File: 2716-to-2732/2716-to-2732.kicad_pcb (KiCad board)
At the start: 2 copper layers, 21.9 x 40.6 mm, 4 parts, among them J1 2716, J2 2732, SW1 A_{11} Select

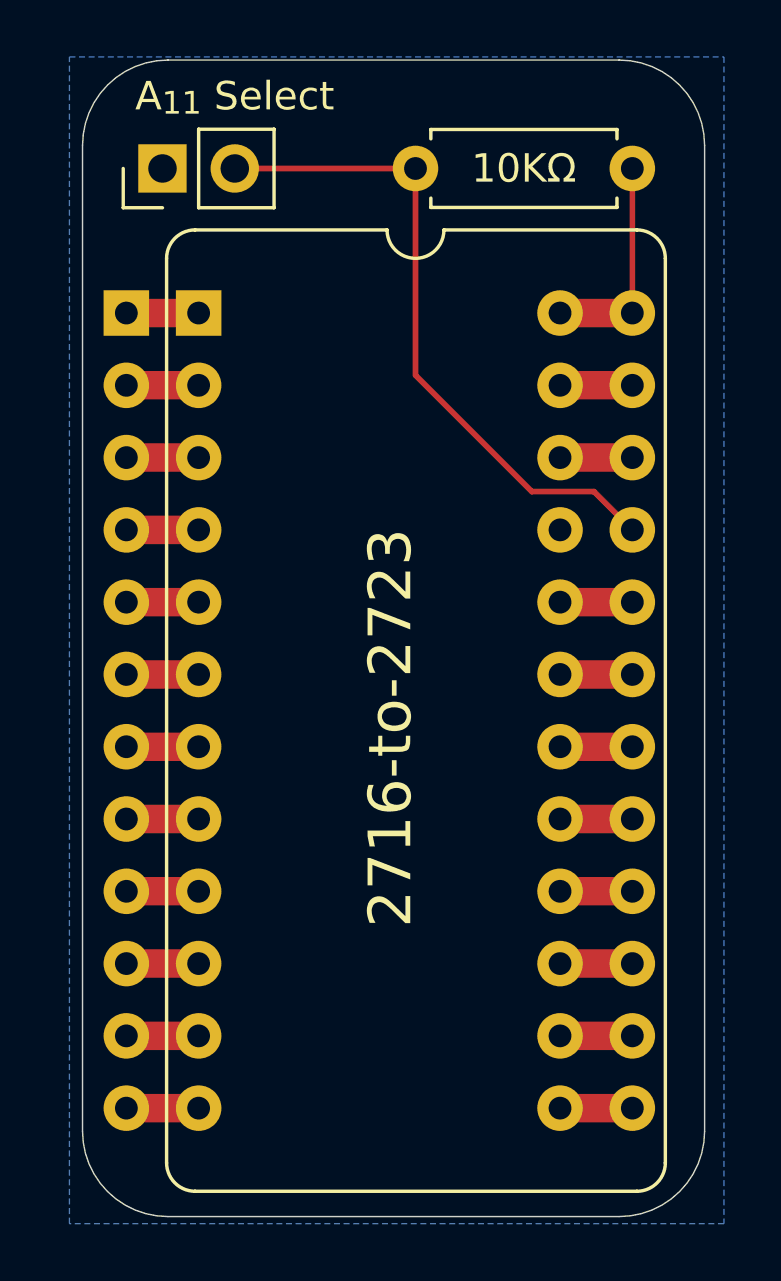
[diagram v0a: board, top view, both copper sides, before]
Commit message: PCB silkscreen update
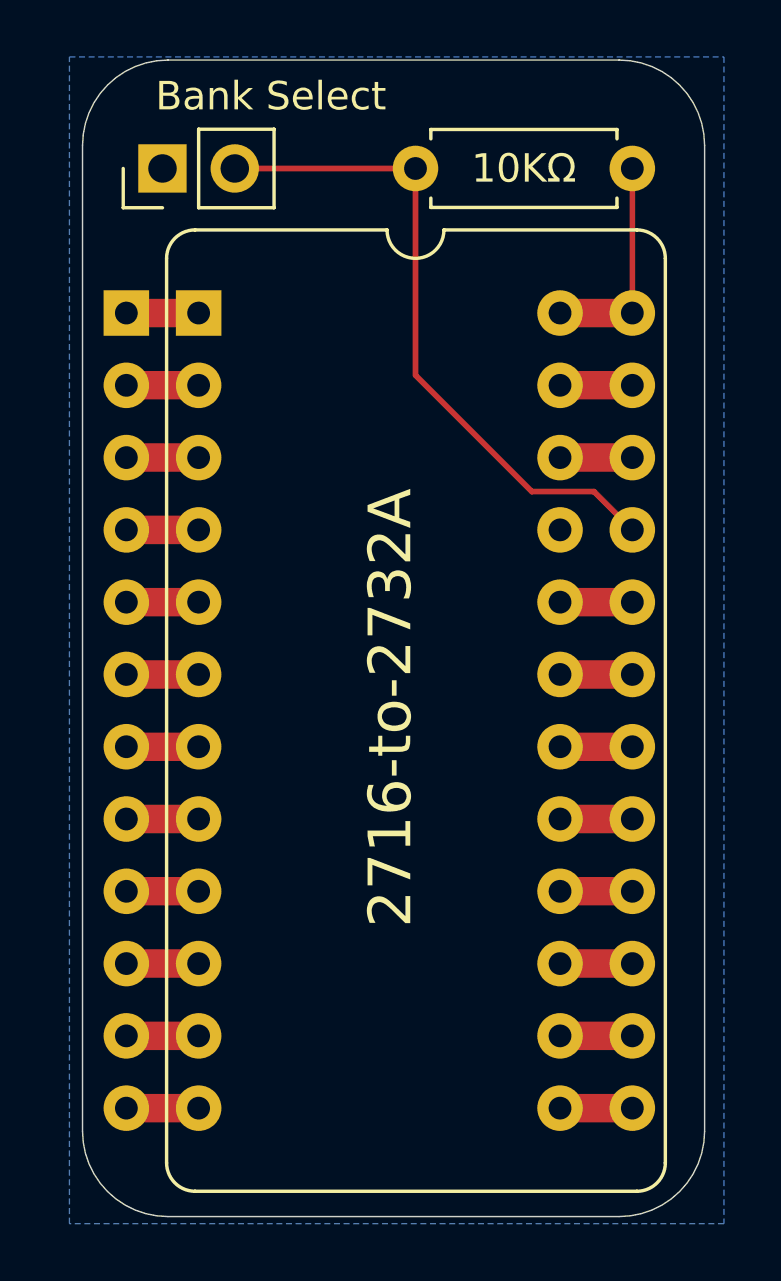
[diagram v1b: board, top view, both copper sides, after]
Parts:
- SW1: value A_{11} Select -> Bank Select
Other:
- board text added: "2716-to-2732A"
- board text removed: "2716-to-2723"
